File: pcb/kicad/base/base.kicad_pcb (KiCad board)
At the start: 2 copper layers, 493 parts, among them P1 J-Link SWD, P10 CONN_01X02, P11 CONN_01X02, P2 SMA, P3 CONN_01X02, P4 USB Micro B, P5 Button, P6 Button, P7 Button, P8 Button, P9 Button, Q1 IRLML2502, U1 SAMB11G18A-edit, U2 XBee-PRO_900HP, Y1 32.768kHz, Y2 26MHz

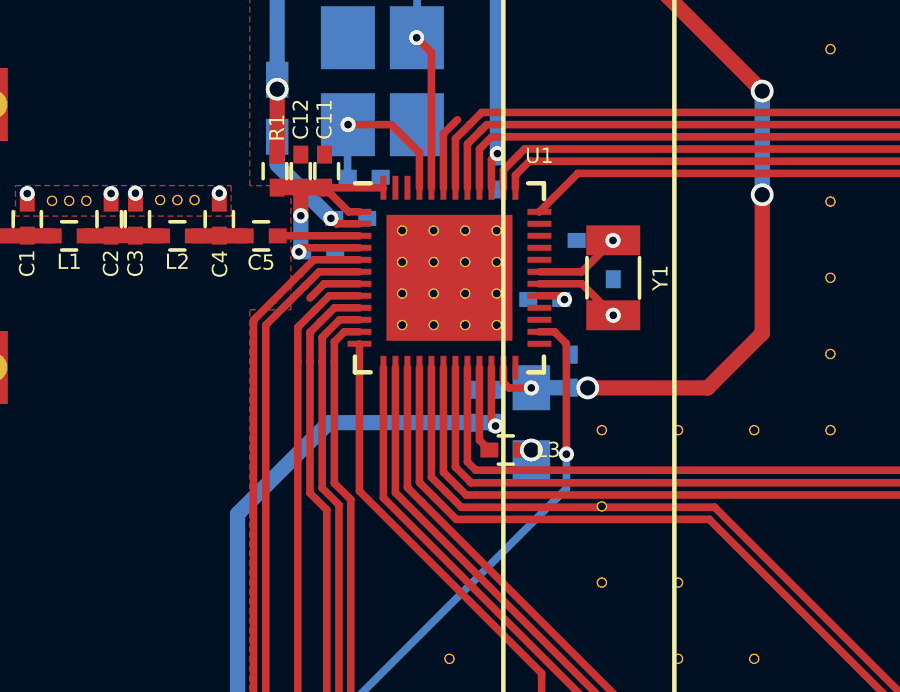
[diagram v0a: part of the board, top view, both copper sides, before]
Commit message: Fix BAC DFM flagged errors
Slight change to copper clearance and specific via pads.
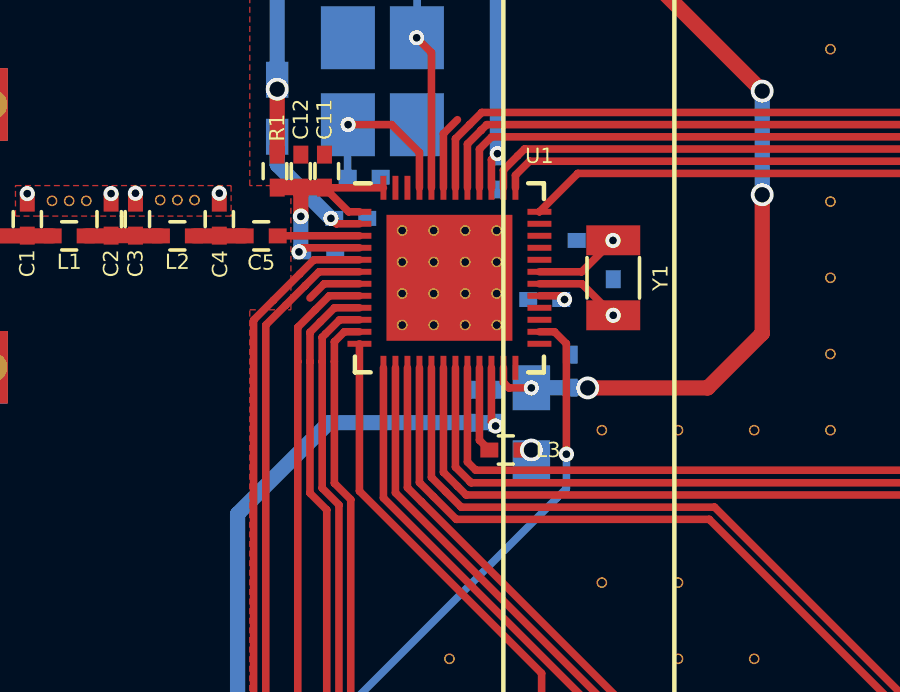
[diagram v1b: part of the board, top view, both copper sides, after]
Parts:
- removed the REF** at (135.1, 78.4)
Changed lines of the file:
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@@
 (kicad_pcb (version 4) (host pcbnew 4.0.5)
   (general
-    (links 607)
+    (links 606)
     (no_connects 0)
     (area 98.626099 29.574066 272.295714 194.39)
@@
     (tracks 302)
     (zones 0)
-    (modules 493)
+    (modules 492)
     (nets 82)
   )
@@
   )
   (setup
-    (last_trace_width 0.508)
+    (last_trace_width 0.254)
     (user_trace_width 0.254)
     (user_trace_width 0.508)
     (user_trace_width 0.762)
     (trace_clearance 0.1397)
-    (zone_clearance 0.1397)
+    (zone_clearance 0.1524)
     (zone_45_only yes)
     (trace_min 0.127)
@@
     (via_min_drill 0.254)
     (user_via 0.508 0.254)
+    (user_via 0.5334 0.254)
     (user_via 0.762 0.508)
     (user_via 0.889 0.635)
@@
   )
   (module Misc:Via_Stitch_Dia0.356mm_Drill0.254mm (layer F.Cu)
-    (at 135.1026 78.359)
-    (fp_text reference REF** (at 0 0.889) (layer F.SilkS) hide
-      (effects (font (size 1 1) (thickness 0.15)))
-    )
-    (fp_text value Via_Stitch_Dia0.356mm_Drill0.254mm (at 0 -0.889) (layer F.Fab)
-      (effects (font (size 1 1) (thickness 0.15)))
-    )
-    (pad 1 thru_hole circle (at 0 0) (size 0.356 0.356) (drill 0.254) (layers *.Cu)
-      (net 2 GND) (zone_connect 2))
-  )
-  (module Misc:Via_Stitch_Dia0.356mm_Drill0.254mm (layer F.Cu)
     (at 135.1026 80.899)
     (fp_text reference REF** (at 0 0.889) (layer F.SilkS) hide
@@
   (segment (start 125.0696 67.733) (end 124.2822 67.733) (width 0.508) (layer F.Cu) (net 10))
   (segment (start 127.8226 67.739) (end 125.863 67.739) (width 0.254) (layer F.Cu) (net 10))
-  (segment (start 125.068806 69.827706) (end 125.068806 68.669694) (width 0.508) (layer B.Cu) (net 10))
-  (via (at 125.068806 68.669694) (size 0.508) (drill 0.254) (layers F.Cu B.Cu) (net 10))
-  (segment (start 125.068806 68.669694) (end 125.0696 68.6689) (width 0.508) (layer F.Cu) (net 10))
-  (segment (start 125.0696 68.6689) (end 125.0696 67.733) (width 0.508) (layer F.Cu) (net 10))
+  (segment (start 125.068806 69.827706) (end 125.0696 68.6943) (width 0.508) (layer B.Cu) (net 10))
+  (via (at 125.0696 68.6943) (size 0.5334) (drill 0.254) (layers F.Cu B.Cu) (net 10))
+  (segment (start 125.0696 68.6943) (end 125.070394 68.693506) (width 0.508) (layer F.Cu) (net 10))
+  (segment (start 125.070394 68.693506) (end 125.0696 67.733) (width 0.508) (layer F.Cu) (net 10))
   (segment (start 127.0226 69.739) (end 125.1425 69.739) (width 0.254) (layer F.Cu) (net 10))
   (via (at 125.0061 69.8754) (size 0.508) (drill 0.254) (layers F.Cu B.Cu) (net 10))
@@
   )
   (zone (net 2) (net_name GND) (layer B.Cu) (hatch edge 0.508)
-    (connect_pads thru_hole_only (clearance 0.1397))
-    (min_thickness 0.1397)
+    (connect_pads thru_hole_only (clearance 0.1524))
+    (min_thickness 0.1524)
     (fill yes (mode segment) (arc_segments 32) (thermal_gap 0.508) (thermal_bridge_width 0.508))
     (polygon
@@
   )
   (zone (net 2) (net_name GND) (layer F.Cu) (hatch edge 0.508)
-    (connect_pads thru_hole_only (clearance 0.1397))
-    (min_thickness 0.1397)
+    (connect_pads thru_hole_only (clearance 0.1524))
+    (min_thickness 0.1524)
     (fill yes (mode segment) (arc_segments 32) (thermal_gap 0.508) (thermal_bridge_width 0.508))
     (polygon

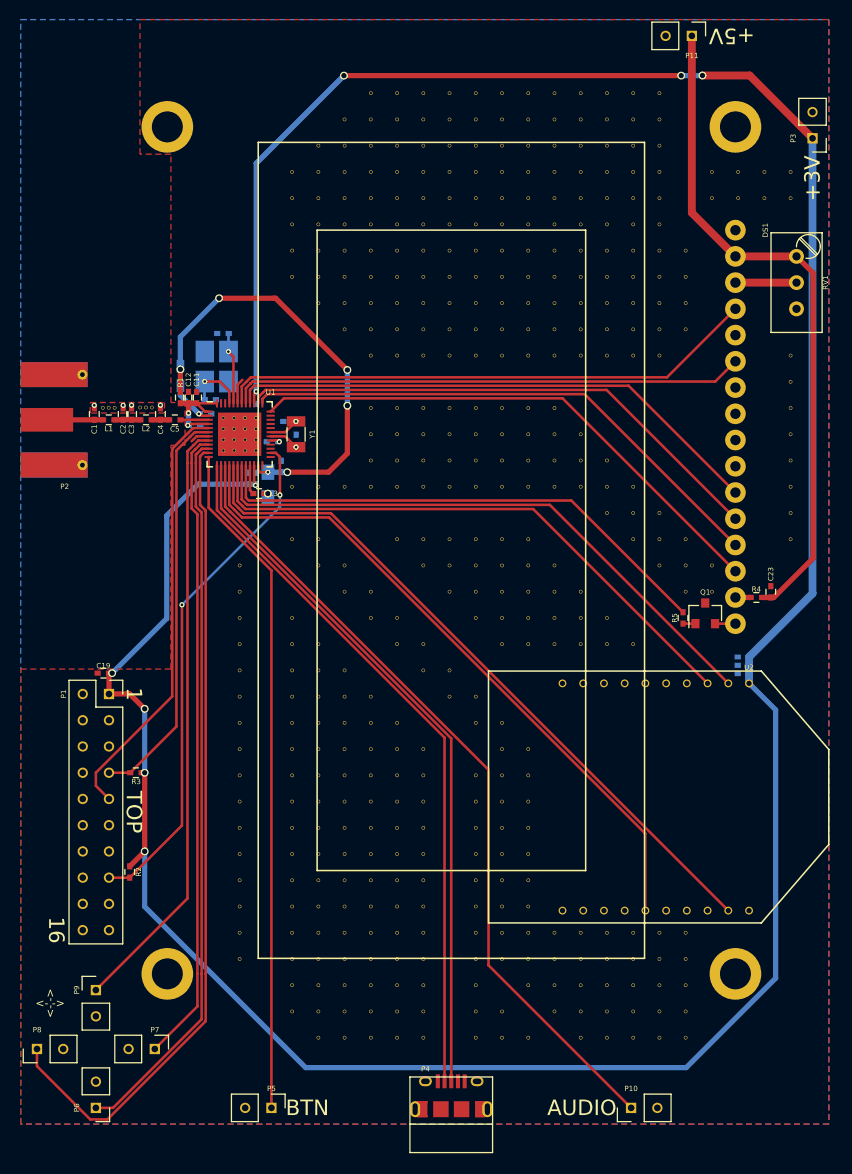
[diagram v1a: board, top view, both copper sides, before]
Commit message: Merge base board with power traces
Cleanup power elements and removed some vias to comply with drill hole
board density.
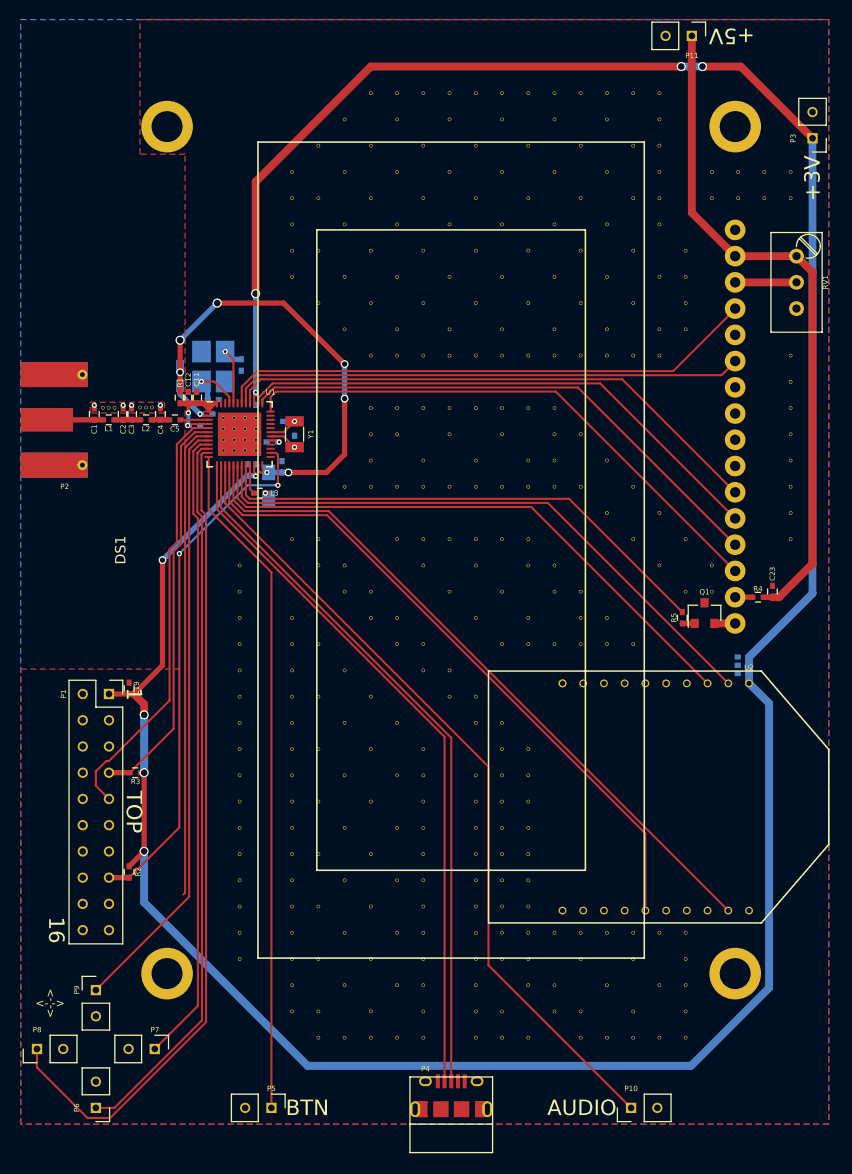
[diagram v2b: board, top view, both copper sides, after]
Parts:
- removed the REF** at (145.3, 121.5)
- removed the REF** at (140.2, 121.5)
- removed the REF** at (142.7, 119.0)
- removed the REF** at (137.6, 119.0)
- removed the REF** at (140.2, 116.5)
- removed the REF** at (145.3, 116.5)
- removed the REF** at (142.7, 124.1)
- removed the REF** at (137.6, 124.1)
- removed the REF** at (140.2, 126.6)
- removed the REF** at (145.3, 126.6)
- removed the REF** at (142.7, 113.9)
- removed the REF** at (137.6, 113.9)
- removed the REF** at (145.3, 111.4)
- removed the REF** at (140.2, 111.4)
- removed the REF** at (137.6, 108.8)
- removed the REF** at (142.7, 108.8)
- removed the REF** at (158.0, 86.0)
- removed the REF** at (160.5, 88.5)
- removed the REF** at (155.4, 88.5)
- removed the REF** at (152.9, 86.0)
- removed the REF** at (155.4, 83.4)
- removed the REF** at (150.3, 83.4)
- removed the REF** at (137.6, 93.6)
- removed the REF** at (145.3, 101.2)
- removed the REF** at (140.2, 101.2)
- removed the REF** at (137.6, 103.8)
- removed the REF** at (142.7, 103.8)
- removed the REF** at (142.7, 98.7)
- removed the REF** at (137.6, 98.7)
- removed the REF** at (140.2, 96.1)
- removed the REF** at (140.2, 106.3)
- removed the REF** at (145.3, 106.3)
- removed the REF** at (173.2, 83.4)
- removed the REF** at (165.6, 75.8)
- removed the REF** at (168.1, 78.4)
- removed the REF** at (170.7, 80.9)
- removed the REF** at (170.7, 126.6)
- removed the REF** at (137.6, 75.8)
- removed the REF** at (135.1, 75.8)
- removed the REF** at (163.0, 73.3)
- removed the REF** at (145.3, 73.3)
- removed the REF** at (150.3, 73.3)
- removed the REF** at (155.4, 73.3)
- removed the REF** at (165.6, 126.6)
- removed the REF** at (158.0, 70.7)
- removed the REF** at (152.9, 70.7)
- removed the REF** at (147.8, 70.7)
- removed the REF** at (137.6, 45.3)
- removed the REF** at (137.6, 55.5)
- removed the REF** at (137.6, 50.4)
- removed the REF** at (163.0, 124.1)
- removed the REF** at (168.1, 60.6)
- removed the REF** at (163.0, 60.6)
- removed the REF** at (168.1, 124.1)
- removed the REF** at (147.8, 60.6)
- removed the REF** at (142.7, 60.6)
- removed the REF** at (152.9, 60.6)
- removed the REF** at (158.0, 60.6)
- removed the REF** at (170.7, 58.0)
- removed the REF** at (165.6, 58.0)
- removed the REF** at (160.5, 58.0)
- removed the REF** at (145.3, 58.0)
- removed the REF** at (140.2, 58.0)
- removed the REF** at (150.3, 58.0)
- removed the REF** at (155.4, 58.0)
- removed the REF** at (165.6, 47.9)
- removed the REF** at (160.5, 47.9)
- removed the REF** at (145.3, 47.9)
- removed the REF** at (140.2, 47.9)
- removed the REF** at (150.3, 47.9)
- removed the REF** at (155.4, 47.9)
- removed the REF** at (158.0, 50.4)
- removed the REF** at (152.9, 50.4)
- removed the REF** at (142.7, 50.4)
- removed the REF** at (147.8, 50.4)
- removed the REF** at (163.0, 50.4)
- removed the REF** at (168.1, 50.4)
- removed the REF** at (168.1, 55.5)
- removed the REF** at (163.0, 55.5)
- removed the REF** at (147.8, 55.5)
- removed the REF** at (142.7, 55.5)
- removed the REF** at (152.9, 55.5)
- removed the REF** at (158.0, 55.5)
- removed the REF** at (155.4, 53.0)
- removed the REF** at (150.3, 53.0)
- removed the REF** at (140.2, 53.0)
- removed the REF** at (145.3, 53.0)
- removed the REF** at (160.5, 53.0)
- removed the REF** at (165.6, 53.0)
- removed the REF** at (170.7, 53.0)
- removed the REF** at (165.6, 42.8)
- removed the REF** at (160.5, 42.8)
- removed the REF** at (145.3, 42.8)
- removed the REF** at (140.2, 42.8)
- removed the REF** at (150.3, 42.8)
- removed the REF** at (155.4, 42.8)
- removed the REF** at (158.0, 45.3)
- removed the REF** at (165.6, 121.5)
- removed the REF** at (152.9, 45.3)
- removed the REF** at (142.7, 45.3)
- removed the REF** at (147.8, 45.3)
- removed the REF** at (163.0, 45.3)
- removed the REF** at (168.1, 45.3)
- removed the REF** at (168.1, 40.3)
- removed the REF** at (163.0, 40.3)
- removed the REF** at (147.8, 40.3)
- removed the REF** at (142.7, 40.3)
- removed the REF** at (152.9, 40.3)
- removed the REF** at (158.0, 40.3)
- removed the REF** at (170.7, 121.5)
- removed the REF** at (160.5, 121.5)
- moved C8 3.53 mm to (130.2, 64.0), turned to 270 degrees
- moved C19 2.90 mm to (119.3, 95.3), turned to 90 degrees
- moved C17 0.83 mm to (131.6, 74.2)
- moved C16 0.83 mm to (130.8, 74.2)
- moved Y2 0.32 mm to (127.5, 64.2)
- moved C9 0.29 mm to (127.5, 67.4)
- moved C6 0.18 mm to (135.3, 71.4)
- moved C23 0.16 mm to (181.6, 86.0)
- moved R4 0.16 mm to (180.2, 86.5)
- moved Y1 0.15 mm to (135.3, 70.7)
- moved C13 0.11 mm to (126.8, 68.8)
- moved C15 0.11 mm to (131.6, 67.3)
- moved L4 0.09 mm to (132.8, 75.7)
- moved C14 0.08 mm to (134.1, 73.9)
- moved L3 0.08 mm to (132.0, 76.4)
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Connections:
- DS1 pad 17: GND -> (no net)
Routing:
- net Net-(U1-Pad7): track 1.84 -> 46.1 mm
- net /+3.3V: track 296.3 -> 291.8 mm
- net /DISP_CTRST: track 2.46 -> 0.00 mm
- net Net-(P1-Pad15): track 49.8 -> 51.4 mm
- net /DISP_B3: track 52.5 -> 53.8 mm
- net Net-(C10-Pad1): track 9.21 -> 10.3 mm
- net /DISP_B0: track 52.7 -> 53.2 mm
- net /DISP_B2: track 52.5 -> 53.0 mm
- net Net-(C14-Pad1): track 43.6 -> 43.9 mm, vias 6 -> 7
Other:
- net class Default: clearance 0.1397 -> 0.1905; trace_width 0.254 -> 0.2032
- net class Power: clearance 0.1397 -> 0.1905
- rule trace_clearance: 0.1397 -> 0.1905
- rule via_min_size: 0.254 -> 0.508

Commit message: Update display, XBee, and USB trace widths
Experimenting with new design constraints of 0.75mil clearance and
0.8mil signal trace widths.
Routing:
- net (no net): track 0.00 -> 8.08 mm, vias 0 -> 1
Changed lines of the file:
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@@
     (user_via 0.508 0.254)
     (user_via 0.762 0.508)
-    (user_via 0.889 0.635)
     (uvia_size 0.3)
     (uvia_drill 0.1)
@@
     (effects (font (size 1.5 1.5) (thickness 0.3)))
   )
+  (segment (start 140.4493 67.9704) (end 140.4493 64.516) (width 0.508) (layer B.Cu) (net 0))
+  (via (at 140.4493 67.9704) (size 0.762) (drill 0.508) (layers F.Cu B.Cu) (net 0))
+  (segment (start 140.4493 72.5932) (end 140.4493 67.9704) (width 0.508) (layer F.Cu) (net 0))
   (segment (start 111.3608 69.342) (end 115.9422 69.342) (width 0.508) (layer F.Cu) (net 1))
   (segment (start 115.9422 69.342) (end 115.951 69.3332) (width 0.508) (layer F.Cu) (net 1))
